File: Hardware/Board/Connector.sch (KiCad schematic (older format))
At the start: 168 parts, among them J300 734-264, J301 733-368, J302 733-368, J303 733-368, J304 Truma, J305 Dormetic, J306 733-368, J307 Conn_01x04, J308 Conn_01x04, J309 733-368, J310 Conn_01x04, J311 Conn_01x04, J312 733-366, J313 733-366, J314 733-370, J315 734-163, J316 733-363, J316 734-163, J317 734-163, J318 734-163, J319 734-168, J321 615008138221, J322 615008138221, J323 Spare, J324 SENSOR, J325 Wasser, J326 Abwasser, J327 733-370, J328 Raspberry_Pi_2_3, J329 733-366, J330 Waveshare IoT Hat, J331 734-168, J400 USB_B_Micro, J401 Dormetic, J500 SENSOR, K300 5-1393243-2, K301 5-1393243-2, K302 5-1393243-2, K303 5-1393243-2, SW300 SW_DIP_x01, SW400 SW_DIP_x01, U300 max4896atp+, U301 max4896atp+, U302 SN65HVD234, U303 ESP-12F, U304 SN65HVD234, U400 USBLC6-2SC6, U401 FT232RL, U402 SN65HVD234, U500 BME680, U501 LSM303AGR

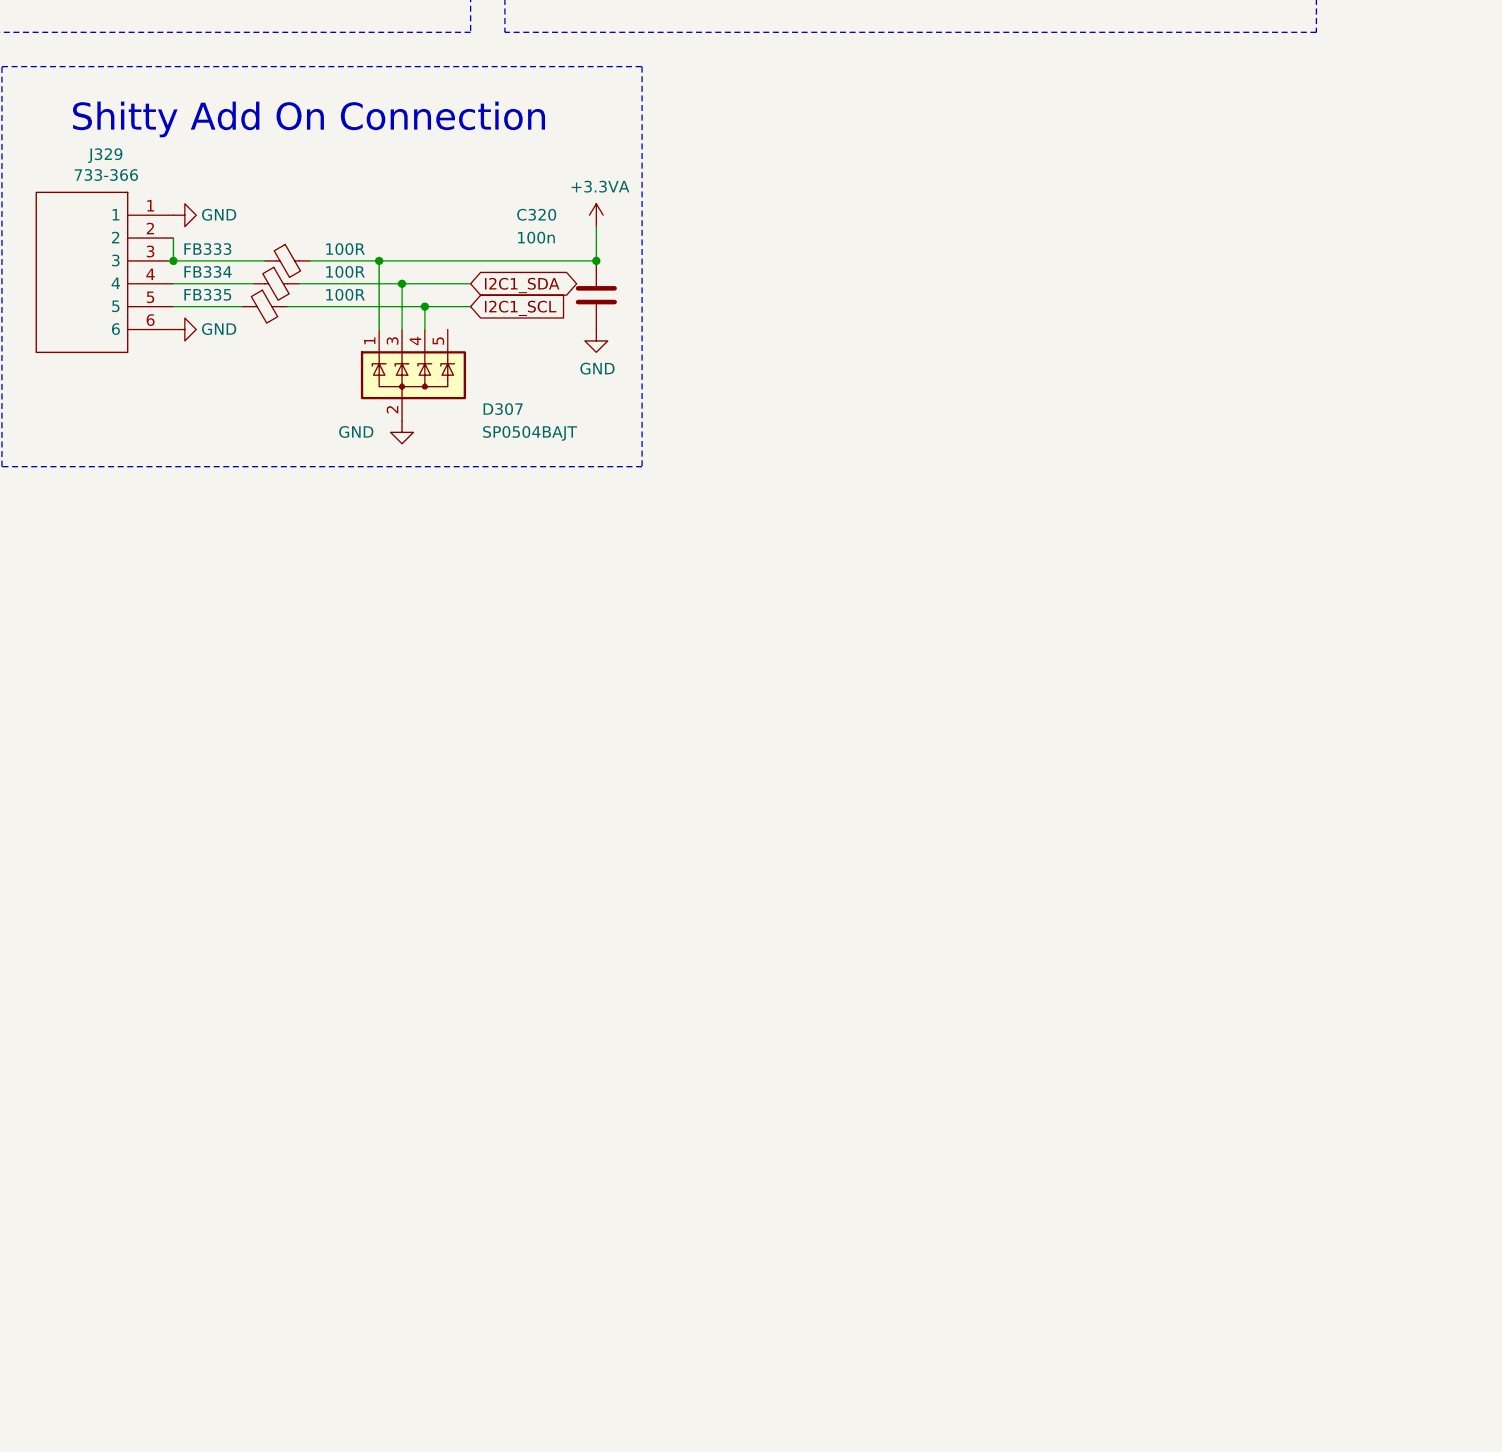
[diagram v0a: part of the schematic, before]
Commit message: Patch LIB mit Netzwerk Bauteilen, ESP32 und PY hinzu gefügt, PI Netzteil auf 5A
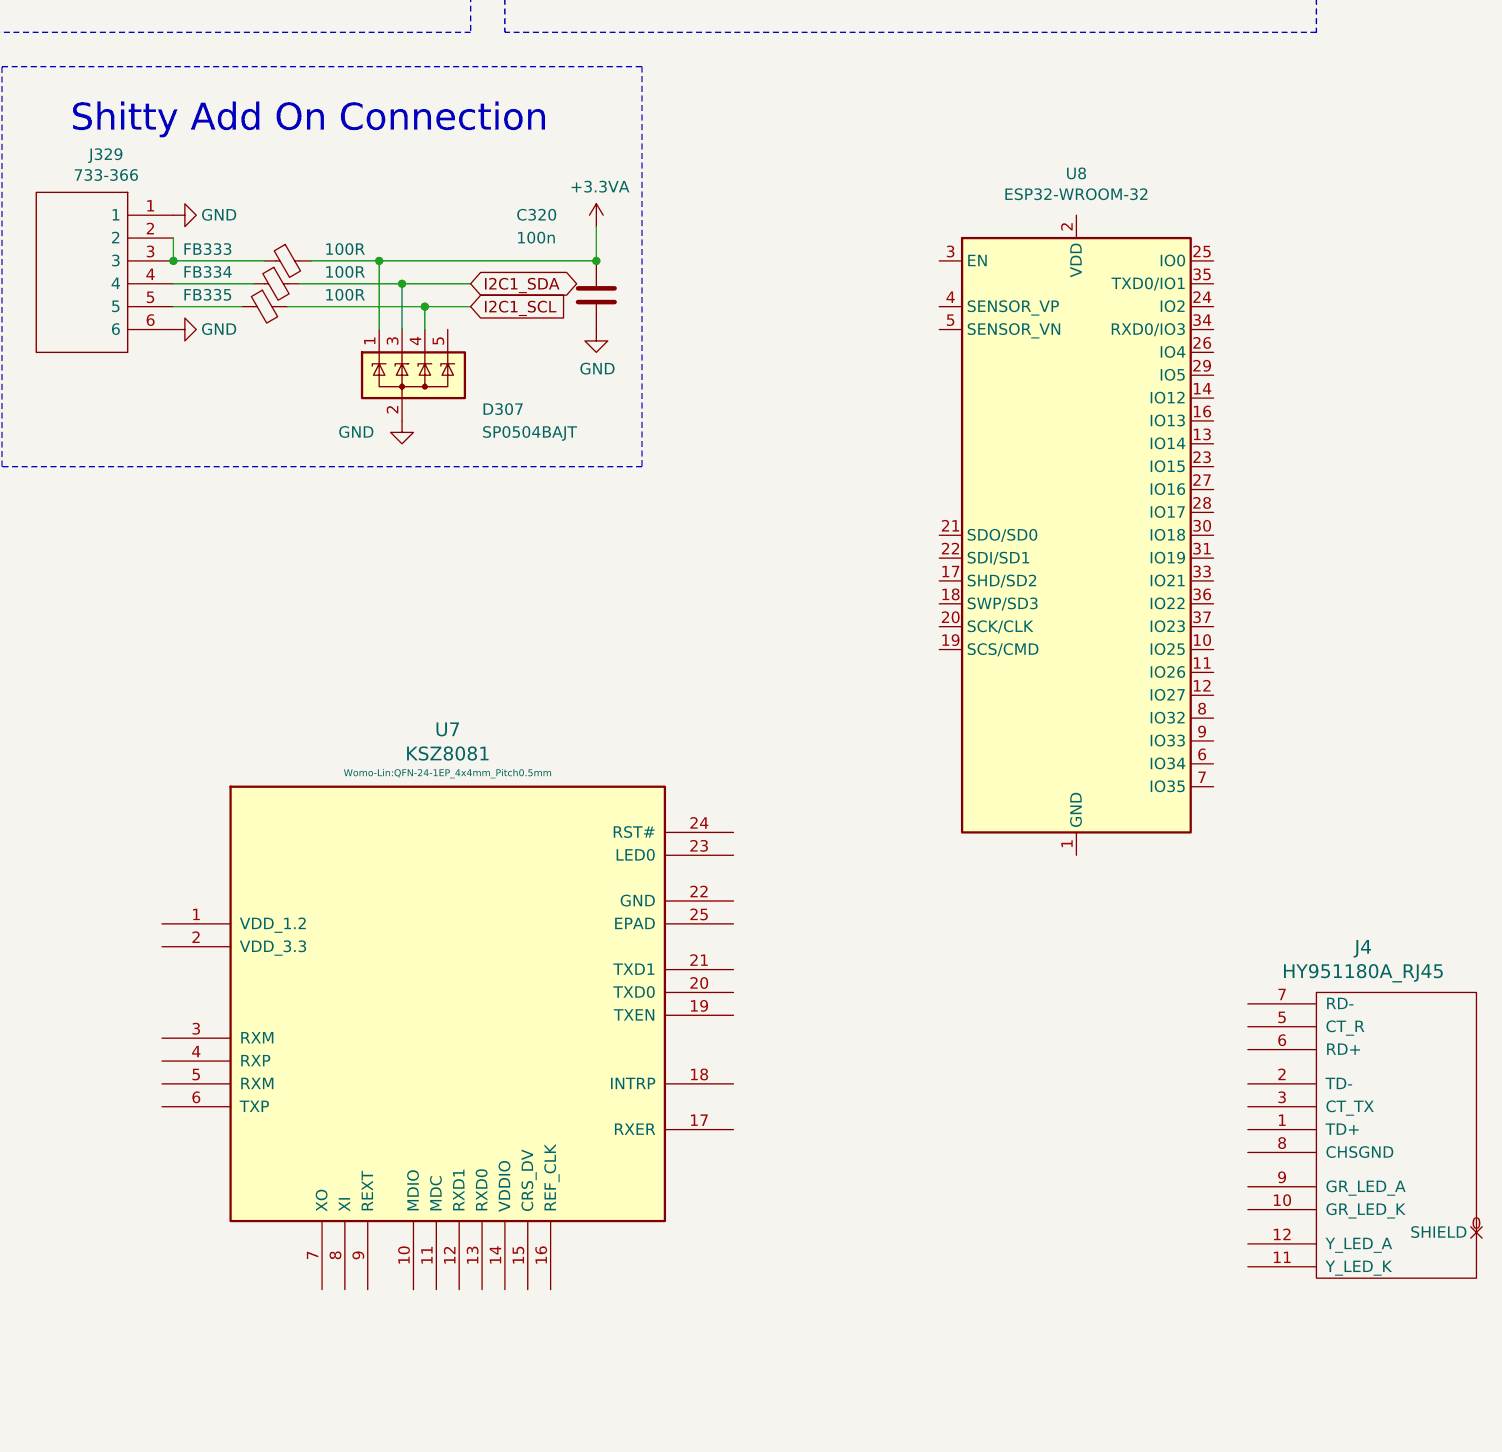
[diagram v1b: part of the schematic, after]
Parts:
- added J4: HY951180A_RJ45, Womo-Lin:HR911105_RJ45, symbol Womo-Lin:HY951180A_RJ45
- added U7: KSZ8081, Womo-Lin:QFN-24-1EP_4x4mm_Pitch0.5mm, symbol Womo-Lin:KSZ8081
- added U8: ESP32-WROOM-32, RF_Module:ESP32-WROOM-32, symbol RF_Module:ESP32-WROOM-32
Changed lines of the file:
@@
 	7650 3200 7650 2800
 Connection ~ 7300 3200
+$Comp
+L RF_Module:ESP32-WROOM-32 U8
+U 1 1 6175766D
+P 19550 10350
+F 0 "U8" H 19550 11931 50  0000 C CNN
+F 1 "ESP32-WROOM-32" H 19550 11840 50  0000 C CNN
+F 2 "RF_Module:ESP32-WROOM-32" H 19550 8850 50  0001 C CNN
+F 3 "https://www.espressif.com/sites/default/files/documentation/esp32-wroom-32_datasheet_en.pdf" H 19250 10400 50  0001 C CNN
+	1    19550 10350
+	1    0    0    -1
+$EndComp
+$Comp
+L Womo-Lin:KSZ8081 U7
+U 1 1 6197849E
+P 16800 12400
+F 0 "U7" H 16800 13599 60  0000 C CNN
+F 1 "KSZ8081" H 16800 13493 60  0000 C CNN
+F 2 "Womo-Lin:QFN-24-1EP_4x4mm_Pitch0.5mm" H 16800 13410 30  0000 C CNN
+F 3 "" H 16800 12400 60  0000 C CNN
+	1    16800 12400
+	1    0    0    -1
+$EndComp
+$Comp
+L Womo-Lin:HY951180A_RJ45 J4
+U 1 1 61981448
+P 20850 12900
+F 0 "J4" H 20805 13647 60  0000 C CNN
+F 1 "HY951180A_RJ45" H 20805 13541 60  0000 C CNN
+F 2 "Womo-Lin:HR911105_RJ45" H 20850 12900 60  0001 C CNN
+F 3 "" H 20850 12900 60  0001 C CNN
+	1    20850 12900
+	1    0    0    -1
+$EndComp
 $EndSCHEMATC

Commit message: Anbindung Raspberry Shield, ESP32 Netzwerk PHY forrtgesetzt
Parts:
- added C?: 22u, Capacitor_SMD:C_1206_3216Metric, symbol Womo-rescue:C-Device
- added C? (x2): 100n, Capacitor_SMD:C_1206_3216Metric, symbol Womo-rescue:C-Device
- added C?: 10u, Capacitor_SMD:C_1206_3216Metric, symbol Womo-rescue:C-Device
- added C?: 2u2, Capacitor_SMD:C_1206_3216Metric, symbol Womo-rescue:C-Device
- added C? (x2): 100n, Capacitor_SMD:C_0603_1608Metric, symbol Womo-rescue:C-Device
- added D?: BAT54C, Package_TO_SOT_SMD:SOT-23, symbol Diode:BAT54C
- added FB?: 100R, Inductor_SMD:L_0603_1608Metric, symbol Womo-rescue:Ferrite_Bead_Small-Device
- added Q? (x2): MMBT3904, Package_TO_SOT_SMD:SOT-23, symbol Transistor_BJT:MMBT3904
- added R? (x3): 330, Resistor_SMD:R_0603_1608Metric, symbol Womo-rescue:R-Device
- added R?: 6k49, Resistor_SMD:R_0603_1608Metric, symbol Womo-rescue:R-Device
- added R? (x4): 51R1, Resistor_SMD:R_0603_1608Metric, symbol Womo-rescue:R-Device
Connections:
- net labels added: EMAC_CLK_OUT, EMAC_RXCRS_DV, EMAC_RXD0, EMAC_RXD1, EMAC_TXD0, EMAC_TXD1, EMAC_TX_EN, ESP_DTR, ESP_RTS, MDC(RMII), MDIO(RMII), RASPI_3V3, RASPI_GPIO10_MOSI0, RASPI_GPIO11_SCLK0, RASPI_GPIO12_PWM0, RASPI_GPIO13_PWM1, RASPI_GPIO16, RASPI_GPIO18_PWM0, RASPI_GPIO19_MISO1, RASPI_GPIO20_MOSI1, RASPI_GPIO21_SCLK1, RASPI_GPIO22, RASPI_GPIO23, RASPI_GPIO24, RASPI_GPIO25, RASPI_GPIO26, RASPI_GPIO27, RASPI_GPIO2_SDA, RASPI_GPIO3_SCL, RASPI_GPIO4_GCLK0, RASPI_GPIO5_GCLK1, RASPI_GPIO6_GCLK2, RASPI_GPIO7_CE1, RASPI_GPIO8_CE0, RASPI_GPIO9_MISO0, RJ45_LED0, RJ45_LED1, RXM, RXP, TXM, TXP
- net labels removed: +5VL
- wire segments 737 -> 837
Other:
- moved on the sheet: C305, C315, C317, C320, D306, D307, FB331, FB332, FB333, FB334, FB335, J329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

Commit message: ESP32 Netzwerk PHY und SD fertig, SD STM32 auf Micro SD, Womo_LIN Lib mit Micro SD gepatcht
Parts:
- removed J4: HY951180A_RJ45, Womo-Lin:HR911105_RJ45, symbol Womo-Lin:HY951180A_RJ45
- removed U303: ESP-12F, RF_Module:ESP-12E, symbol Womo-rescue:ESP-12F-RF_Module
- removed U7: KSZ8081, Womo-Lin:QFN-24-1EP_4x4mm_Pitch0.5mm, symbol Womo-Lin:KSZ8081
- added C?: 22u, Capacitor_SMD:C_1206_3216Metric, symbol Womo-rescue:C-Device
- added C? (x2): 100n, Capacitor_SMD:C_1206_3216Metric, symbol Womo-rescue:C-Device
- added C?: 100n, Capacitor_SMD:C_0603_1608Metric, symbol Womo-rescue:C-Device
- added C?: 1u, Capacitor_SMD:C_1206_3216Metric, symbol Womo-rescue:C-Device
- added J?: Connector_Micro_SD_Card_Det_Hirose_DM3AT, symbol Womo-Lin:Connector_Micro_SD_Card_Det_Hirose_DM3AT
- added J?: HY951180A_RJ45, symbol Womo-Lin:HY951180A_RJ45
- added R? (x4): 10k, Resistor_SMD:R_0603_1608Metric, symbol Womo-rescue:R-Device
- added R? (x2): 1k5, Resistor_SMD:R_0603_1608Metric, symbol Womo-rescue:R-Device
- added R? (x2): 220, Resistor_SMD:R_0603_1608Metric, symbol Womo-rescue:R-Device
- added R? (x5): 2k2, Resistor_SMD:R_0603_1608Metric, symbol Womo-rescue:R-Device
- added R?: 10, Resistor_SMD:R_0603_1608Metric, symbol Womo-rescue:R-Device
- added SW?: ESP_B, Button_Switch_THT:SW_PUSH_6mm, symbol Womo-rescue:SW_Push-Switch
- added U?: KSZ8081, QFN24, symbol Womo-Lin:KSZ8081
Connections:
- net labels added: +3.3VP, ESP_CTRL_RX, ESP_CTRL_SB, ESP_CTRL_TX, ESP_EN, ESP_GPIO0, ESP_RX, ESP_SD_CS, ESP_SD_DI, ESP_SD_DO, ESP_SD_SCLK, ESP_TX
- net labels removed: ESP_Boot, ESP_Enable, ESP_Reset
- wire segments 837 -> 920
- no-connect marks 16 -> 2
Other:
- note added: "ESP32 with LAN Interface"
- note removed: "ESP with Control Bus"
- moved on the sheet: C315, C317, C?, D?, Q?, R303, R304, R?, U304, U8
